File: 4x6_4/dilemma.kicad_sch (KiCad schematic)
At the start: 342 parts, among them J1 USB_C_Receptacle_USB2.0, J102 NA_serial, J105 NA_Conn_01x04_Female, J113 Cirque, J3 NA_GC9A01, J4 Conn_01x05, J5 NA_Conn_01x02, J5001 USB_C_Receptacle_USB2.0, J5002 NA_Conn_01x02, J5003 NA_serial, J5004 NA_GC9A01, J5005 NA_Conn_01x04_Female, J5007 Cirque, J5008 Conn_01x05, J5009 Conn_01x05, J5010 Conn_01x05, SW1 SW_Push, SW101 NA_SW_Push, SW102 NA_SW_Push, SW103 NA_SW_Push, SW104 NA_SW_Push, SW105 NA_SW_Push, SW106 NA_SW_Push, SW107 NA_SW_Push, SW108 NA_SW_Push, SW109 NA_SW_Push, SW112 NA_SW_Push, SW113 NA_SW_Push, SW114 NA_SW_Push, SW115 NA_SW_Push, SW116 NA_SW_Push, SW117 NA_SW_Push, SW118 NA_SW_Push, SW119 NA_SW_Push, SW3001 NA_SW_Push, SW3002 NA_RotaryEncoder_Switch, SW5001 SW_Push, SW5002 NA_SW_Push, SW5003 NA_SW_Push, SW5004 NA_SW_Push, SW5005 NA_SW_Push, SW5006 NA_SW_Push, SW5007 NA_SW_Push, SW5008 NA_SW_Push, SW5009 NA_SW_Push, SW5010 NA_SW_Push, SW5011 NA_SW_Push, SW5012 NA_SW_Push, SW5013 NA_SW_Push, SW5014 NA_SW_Push, SW5015 NA_SW_Push, SW5016 NA_SW_Push, SW5017 NA_SW_Push, SW5018 NA_SW_Push, SW5019 NA_SW_Push, SW5020 NA_RotaryEncoder_Switch, SW5021 SW_SPST, SW5022 SW_SPST, SW5023 NA_SW_Push, SW5024 NA_SW_Push, SW5025 NA_SW_Push, SW5026 NA_SW_Push, SW5027 NA_SW_Push, SW5028 NA_SW_Push, SW5029 NA_SW_Push, SW5030 NA_SW_Push, SW5031 NA_SW_Push, SW5032 NA_SW_Push, SW5033 NA_SW_Push, SW5034 NA_SW_Push, SW5035 NA_SW_Push, SW5036 NA_SW_Push, SW5037 NA_SW_Push, SW5038 NA_SW_Push, SW5039 NA_SW_Push, SW5040 NA_SW_Push, SW5041 NA_SW_Push, SW5042 NA_SW_Push, U1 RP2040, U2 W25Q128JVS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

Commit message: diodes top
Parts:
- D112, D115, D5002, D5003, D5005, D5006, D5007, D5008, D5009, D5010, D5011, D5012, D5015, D5067, D5068, D5069, D5070, D5071, D5072, D5073, D5074, D5075, D5076, D5077, D5078, D5079, D5080, D5081, D5082, D5083, D5084, D5085, D5086, D5087, D5088, D5089, D5090, D5091, D5092, D5093, D5094, D5095, D5096, D5097, D5098, D5099, D5100, D5101, D5102, D5103, D5104, D5105, D5106, D5107, D5108, D5126: footprint local-libraries:D_0402 -> local-libraries:D_SOD-323

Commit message: update footprints
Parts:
- SW101, SW102, SW103, SW104, SW105, SW106, SW107, SW108, SW109, SW112, SW113, SW114, SW115, SW116, SW117, SW118, SW119, SW3001, SW5002, SW5003, SW5004, SW5005, SW5006, SW5007, SW5008, SW5009, SW5010, SW5011, SW5012, SW5013, SW5014, SW5015, SW5016, SW5017, SW5018, SW5019, SW5023, SW5024, SW5025, SW5026, SW5027, SW5028, SW5029, SW5030, SW5031, SW5032, SW5033, SW5034, SW5035, SW5036, SW5037, SW5038, SW5039, SW5040, SW5041: footprint local-libraries:SW_MX_choc -> local-libraries:Kailh_socket_PG1350
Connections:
- net ~{RESET_L}: now also J5002.2 (Pin_2); no longer SW5001.2
- net ~{RESET}: now also J5.2 (Pin_2); no longer SW1.2
- net at R3.1: now also SW1.2; no longer J5.2 (Pin_2)
- net at R5003.1: now also SW5001.2; no longer J5002.2 (Pin_2)
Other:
- moved on the sheet: D1, D5001, J5, J5002, R1, R2, R3, R5001, R5002, R5003, SW1, SW5001

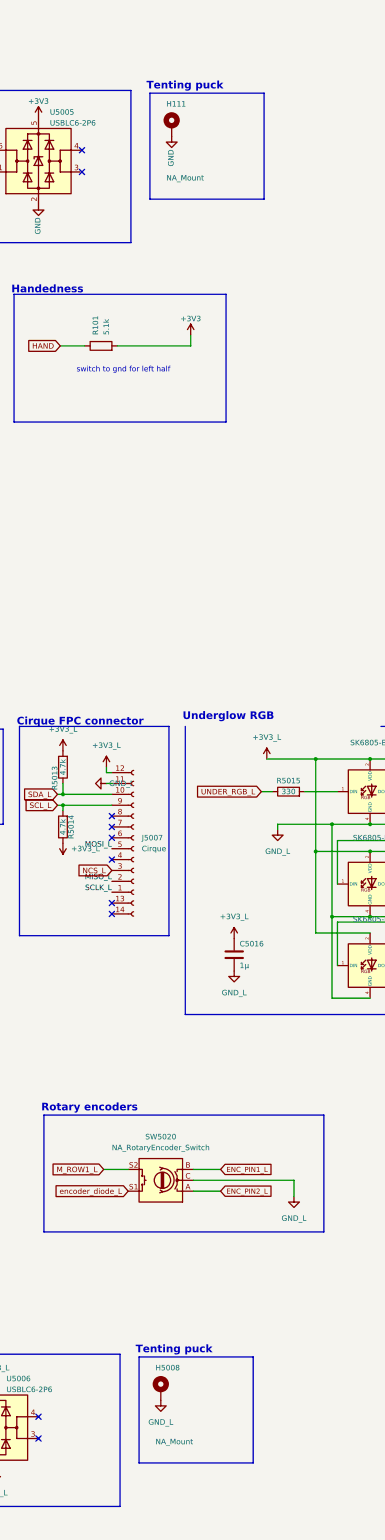
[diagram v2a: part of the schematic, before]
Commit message: north facing leds
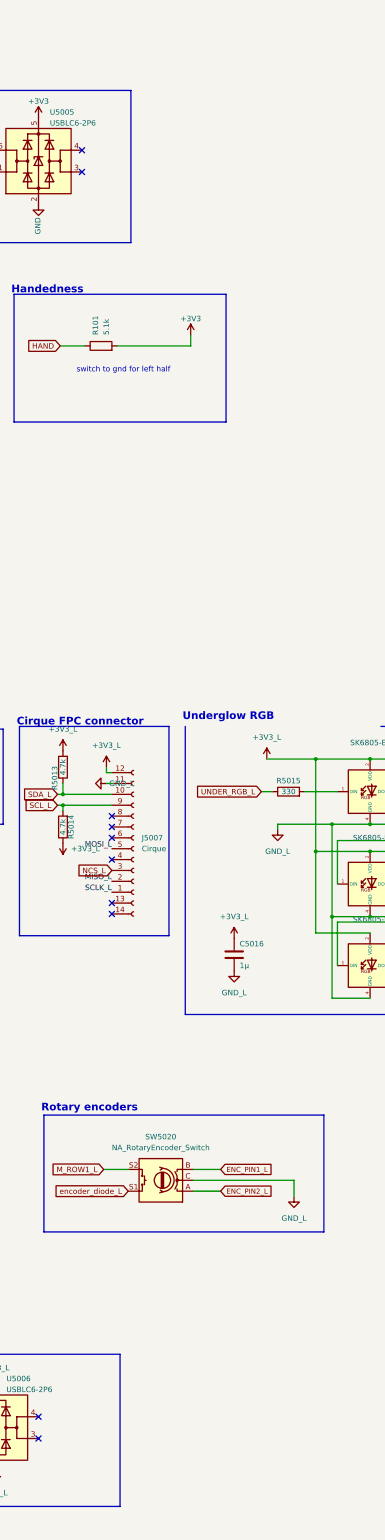
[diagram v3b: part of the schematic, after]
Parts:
- removed H111, H5008: NA_Mount, local-libraries:Tenting_Puck, symbol Mechanical:MountingHole_Pad
- SW5042: footprint local-libraries:SW_MX_choc -> local-libraries:Kailh_socket_PG1350
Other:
- note removed: "Tenting puck"
